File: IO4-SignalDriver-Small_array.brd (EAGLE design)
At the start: 128.3 x 106.7 mm, 71 parts, among them IC1X11 74HS139A, IC1X12 74HS139A, IC1X21 74HS139A, IC1X22 74HS139A

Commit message: added values for connectors
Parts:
- BOARD: value (none) -> 10x10
- CON4X11, CON4X12, CON4X21, CON4X22, CON5X11, CON5X12, CON5X21, CON5X22: value (none) -> 3.5mm
- HEAD1X11, HEAD1X12, HEAD1X21: value Head 1 -> 2mm
- HEAD2X11, HEAD2X21: value Head 2 -> 2mm
- IO4X11, IO4X12, IO4X21, IO4X22: value (none) -> RJ12/6
- renumbered U$2X1 to BOARD
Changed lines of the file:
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@@
 <elements>
 <element name="C1X11" library="SPCoast" package="0805-CAP" value="0.1UF" x="23.225" y="27.686" rot="R270"/>
-<element name="CON4X11" library="SPCoast" package="SCREWTERMINAL-3.5MM-4" value="" x="3.54" y="24.765" rot="R270"/>
-<element name="CON5X11" library="SPCoast" package="SCREWTERMINAL-3.5MM-4" value="" x="3.54" y="42.291" rot="R270"/>
+<element name="CON4X11" library="SPCoast" package="SCREWTERMINAL-3.5MM-4" value="3.5mm" x="3.54" y="24.765" rot="R270"/>
+<element name="CON5X11" library="SPCoast" package="SCREWTERMINAL-3.5MM-4" value="3.5mm" x="3.54" y="42.291" rot="R270"/>
 <element name="FID1X11" library="SPCoast" package="FIDUCIAL_1MM" value="FIDUCIAL" x="47.863" y="8.255"/>
 <element name="FID3X11" library="SPCoast" package="FIDUCIAL_1MM" value="FIDUCIAL" x="8.239" y="43.561"/>
-<element name="HEAD1X11" library="SPCoast" package="4P-2.0" value="Head 1" x="9.89" y="36.195" rot="R270"/>
-<element name="HEAD2X11" library="SPCoast" package="4P-2.0" value="Head 2" x="9.89" y="20.32" rot="R270"/>
+<element name="HEAD1X11" library="SPCoast" package="4P-2.0" value="2mm" x="9.89" y="36.195" rot="R270"/>
+<element name="HEAD2X11" library="SPCoast" package="4P-2.0" value="2mm" x="9.89" y="20.32" rot="R270"/>
 <element name="IC1X11" library="SPCoast" package="SO16" value="74HS139A" x="29.448" y="27.559"/>
-<element name="IO4X11" library="SPCoast" package="RJ25-INVERTED" value="" x="44.815" y="27.94" rot="R90"/>
+<element name="IO4X11" library="SPCoast" package="RJ25-INVERTED" value="RJ12/6" x="44.815" y="27.94" rot="R90"/>
 <element name="R4X11" library="SPCoast" package="0805-RES" value="1k0" x="19.415" y="20.574"/>
 <element name="R6X11" library="SPCoast" package="0805-RES" value="2k2" x="19.415" y="16.764"/>
@@
 <element name="U$2X11" library="SPCoast" package="MOUNTINGHOLE" value="MOUNTINGHOLE" x="43.545" y="44.45"/>
 <element name="C1X12" library="SPCoast" package="0805-CAP" value="0.1UF" x="23.225" y="71.336" rot="R270"/>
-<element name="CON4X12" library="SPCoast" package="SCREWTERMINAL-3.5MM-4" value="" x="3.54" y="68.415" rot="R270"/>
-<element name="CON5X12" library="SPCoast" package="SCREWTERMINAL-3.5MM-4" value="" x="3.54" y="85.941" rot="R270"/>
+<element name="CON4X12" library="SPCoast" package="SCREWTERMINAL-3.5MM-4" value="3.5mm" x="3.54" y="68.415" rot="R270"/>
+<element name="CON5X12" library="SPCoast" package="SCREWTERMINAL-3.5MM-4" value="3.5mm" x="3.54" y="85.941" rot="R270"/>
 <element name="FID1X12" library="SPCoast" package="FIDUCIAL_1MM" value="FIDUCIAL" x="47.863" y="51.905"/>
 <element name="FID3X12" library="SPCoast" package="FIDUCIAL_1MM" value="FIDUCIAL" x="8.239" y="87.211"/>
-<element name="HEAD1X12" library="SPCoast" package="4P-2.0" value="Head 1" x="9.89" y="79.845" rot="R270"/>
+<element name="HEAD1X12" library="SPCoast" package="4P-2.0" value="2mm" x="9.89" y="79.845" rot="R270"/>
 <element name="HEAD2X12" library="SPCoast" package="4P-2.0" value="Head 2" x="9.89" y="63.97" rot="R270"/>
 <element name="IC1X12" library="SPCoast" package="SO16" value="74HS139A" x="29.448" y="71.209"/>
-<element name="IO4X12" library="SPCoast" package="RJ25-INVERTED" value="" x="44.815" y="71.59" rot="R90"/>
+<element name="IO4X12" library="SPCoast" package="RJ25-INVERTED" value="RJ12/6" x="44.815" y="71.59" rot="R90"/>
 <element name="R4X12" library="SPCoast" package="0805-RES" value="1k0" x="19.415" y="64.224"/>
 <element name="R6X12" library="SPCoast" package="0805-RES" value="2k2" x="19.415" y="60.414"/>
@@
 <element name="U$2X12" library="SPCoast" package="MOUNTINGHOLE" value="MOUNTINGHOLE" x="43.545" y="88.1"/>
 <element name="C1X21" library="SPCoast" package="0805-CAP" value="0.1UF" x="73.225" y="27.686" rot="R270"/>
-<element name="CON4X21" library="SPCoast" package="SCREWTERMINAL-3.5MM-4" value="" x="53.54" y="24.765" rot="R270"/>
-<element name="CON5X21" library="SPCoast" package="SCREWTERMINAL-3.5MM-4" value="" x="53.54" y="42.291" rot="R270"/>
+<element name="CON4X21" library="SPCoast" package="SCREWTERMINAL-3.5MM-4" value="3.5mm" x="53.54" y="24.765" rot="R270"/>
+<element name="CON5X21" library="SPCoast" package="SCREWTERMINAL-3.5MM-4" value="3.5mm" x="53.54" y="42.291" rot="R270"/>
 <element name="FID1X21" library="SPCoast" package="FIDUCIAL_1MM" value="FIDUCIAL" x="97.863" y="8.255"/>
 <element name="FID3X21" library="SPCoast" package="FIDUCIAL_1MM" value="FIDUCIAL" x="58.239" y="43.561"/>
-<element name="HEAD1X21" library="SPCoast" package="4P-2.0" value="Head 1" x="59.89" y="36.195" rot="R270"/>
-<element name="HEAD2X21" library="SPCoast" package="4P-2.0" value="Head 2" x="59.89" y="20.32" rot="R270"/>
+<element name="HEAD1X21" library="SPCoast" package="4P-2.0" value="2mm" x="59.89" y="36.195" rot="R270"/>
+<element name="HEAD2X21" library="SPCoast" package="4P-2.0" value="2mm" x="59.89" y="20.32" rot="R270"/>
 <element name="IC1X21" library="SPCoast" package="SO16" value="74HS139A" x="79.448" y="27.559"/>
-<element name="IO4X21" library="SPCoast" package="RJ25-INVERTED" value="" x="94.815" y="27.94" rot="R90"/>
+<element name="IO4X21" library="SPCoast" package="RJ25-INVERTED" value="RJ12/6" x="94.815" y="27.94" rot="R90"/>
 <element name="R4X21" library="SPCoast" package="0805-RES" value="1k0" x="69.415" y="20.574"/>
 <element name="R6X21" library="SPCoast" package="0805-RES" value="2k2" x="69.415" y="16.764"/>
@@
 <element name="U$2X21" library="SPCoast" package="MOUNTINGHOLE" value="MOUNTINGHOLE" x="93.545" y="44.45"/>
 <element name="C1X22" library="SPCoast" package="0805-CAP" value="0.1UF" x="73.225" y="71.336" rot="R270"/>
-<element name="CON4X22" library="SPCoast" package="SCREWTERMINAL-3.5MM-4" value="" x="53.54" y="68.415" rot="R270"/>
-<element name="CON5X22" library="SPCoast" package="SCREWTERMINAL-3.5MM-4" value="" x="53.54" y="85.941" rot="R270"/>
+<element name="CON4X22" library="SPCoast" package="SCREWTERMINAL-3.5MM-4" value="3.5mm" x="53.54" y="68.415" rot="R270"/>
+<element name="CON5X22" library="SPCoast" package="SCREWTERMINAL-3.5MM-4" value="3.5mm" x="53.54" y="85.941" rot="R270"/>
 <element name="FID1X22" library="SPCoast" package="FIDUCIAL_1MM" value="FIDUCIAL" x="97.863" y="51.905"/>
 <element name="FID3X22" library="SPCoast" package="FIDUCIAL_1MM" value="FIDUCIAL" x="58.239" y="87.211"/>
@@
 <element name="HEAD2X22" library="SPCoast" package="4P-2.0" value="Head 2" x="59.89" y="63.97" rot="R270"/>
 <element name="IC1X22" library="SPCoast" package="SO16" value="74HS139A" x="79.448" y="71.209"/>
-<element name="IO4X22" library="SPCoast" package="RJ25-INVERTED" value="" x="94.815" y="71.59" rot="R90"/>
+<element name="IO4X22" library="SPCoast" package="RJ25-INVERTED" value="RJ12/6" x="94.815" y="71.59" rot="R90"/>
 <element name="R4X22" library="SPCoast" package="0805-RES" value="1k0" x="69.415" y="64.224"/>
 <element name="R6X22" library="SPCoast" package="0805-RES" value="2k2" x="69.415" y="60.414"/>
@@
 <element name="U$1X22" library="SPCoast" package="MOUNTINGHOLE" value="MOUNTINGHOLE" x="93.545" y="55.08"/>
 <element name="U$2X22" library="SPCoast" package="MOUNTINGHOLE" value="MOUNTINGHOLE" x="93.545" y="88.1"/>
-<element name="U$2X1" library="SPCoast" package="BOARD-10X10-2X2-PANEL" value="" x="0" y="0"/>
+<element name="BOARD" library="SPCoast" package="BOARD-10X10-2X2-PANEL" value="10x10" x="0" y="0"/>
 <element name="FIDUL" library="SPCoast" package="FIDUCIAL_1MM" value="FIDUCIAL" x="9.509" y="96.101"/>
 <element name="FIDLR" library="SPCoast" package="FIDUCIAL_1MM" value="FIDUCIAL" x="92.059" y="3.391"/>

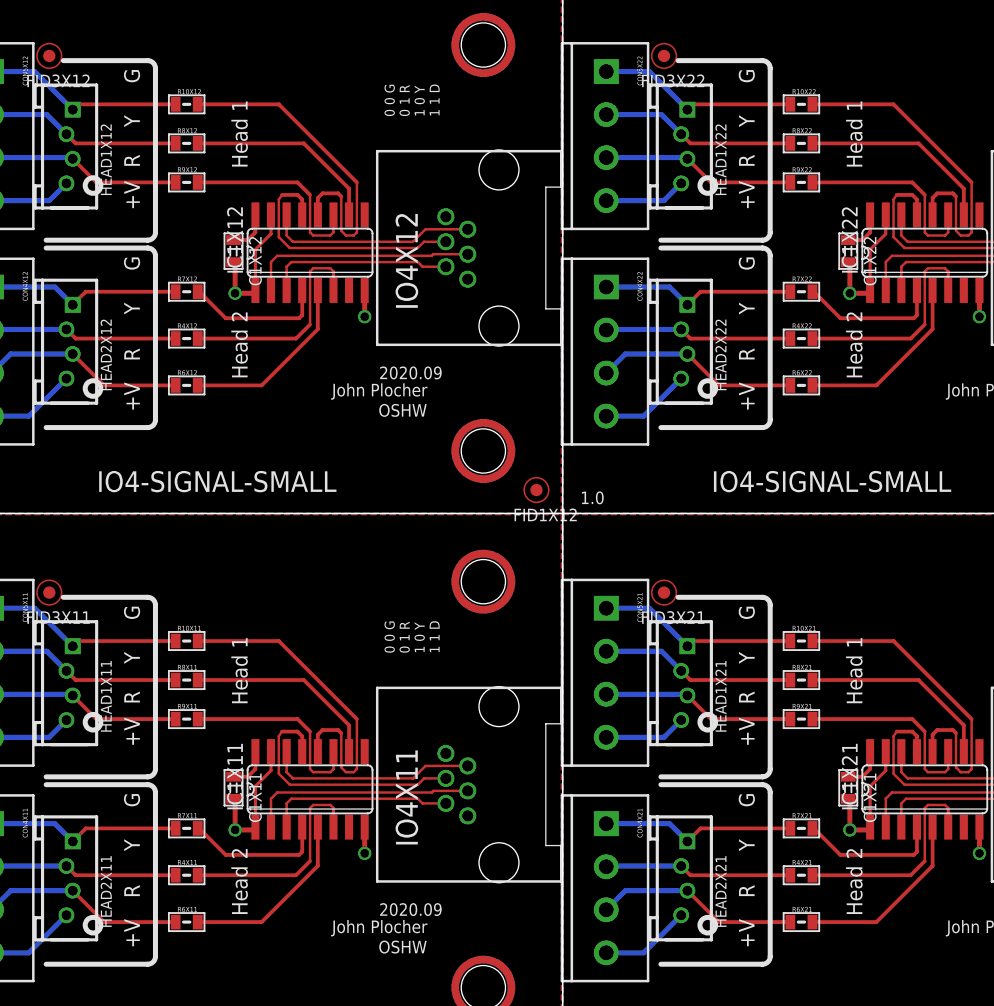
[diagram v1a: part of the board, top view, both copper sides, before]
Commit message: normalized values
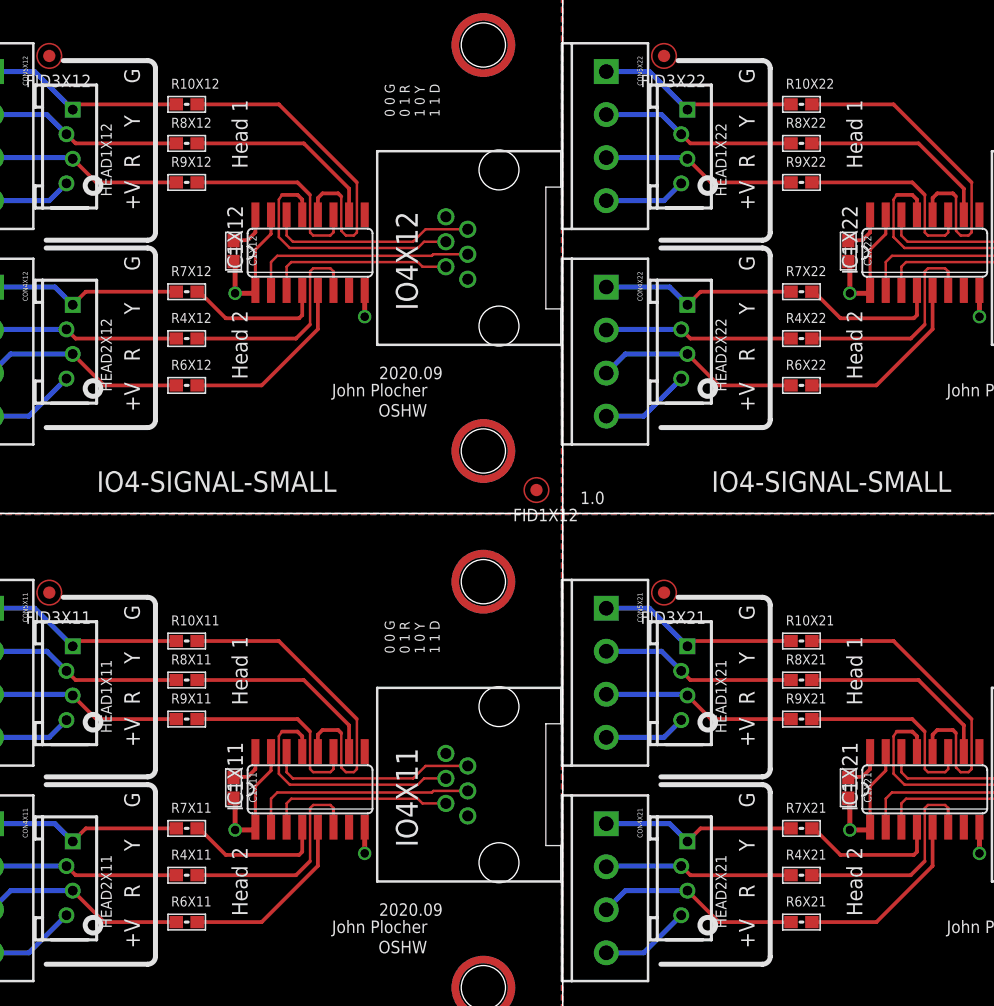
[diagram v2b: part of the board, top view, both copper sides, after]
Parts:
- BOARD: value 10x10 -> BOARD
- C1X11, C1X12, C1X21, C1X22: device SPCoast:0805-CAP -> SPCoast:0603-CAP
- R10X11, R10X12, R10X21, R10X22, R4X11, R4X12, R4X21, R4X22, R6X11, R6X12, R6X21, R6X22, R7X11, R7X12, R7X21, R7X22, R8X11, R8X12, R8X21, R8X22, R9X11, R9X12, R9X21, R9X22: device SPCoast:0805-RES -> SPCoast:0603-RES
